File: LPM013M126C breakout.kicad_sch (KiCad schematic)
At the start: 9 parts, among them J1 Conn_01x12

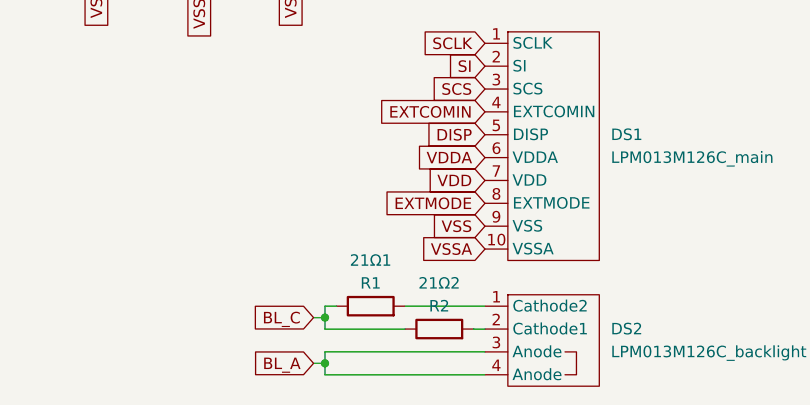
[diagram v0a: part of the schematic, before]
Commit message: fix references for R1, R2
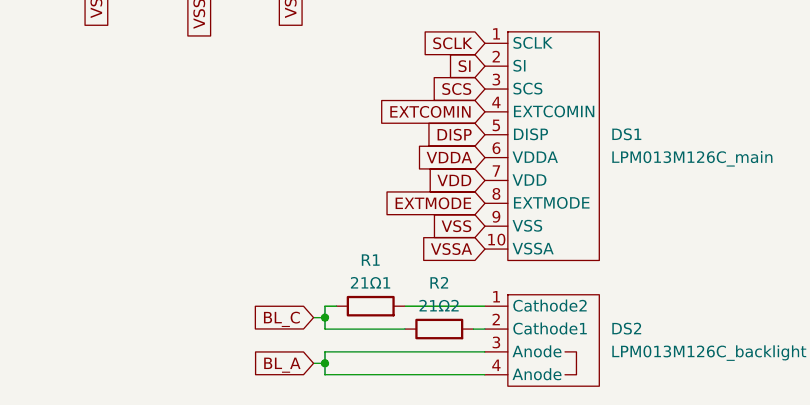
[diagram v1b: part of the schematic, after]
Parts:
- R1: renamed from 21Ω1; value R1 -> 21Ω1
- R2: renamed from 21Ω2; value R2 -> 21Ω2
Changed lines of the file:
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@@
   (symbol (lib_id "Device:R") (at 147.32 121.92 90) (unit 1)
     (in_bom yes) (on_board yes)
-    (property "Reference" "21Ω2" (id 0) (at 147.32 116.84 90))
-    (property "Value" "R2" (id 1) (at 147.32 119.38 90))
+    (property "Reference" "R2" (id 0) (at 147.32 116.84 90))
+    (property "Value" "21Ω2" (id 1) (at 147.32 119.38 90))
     (property "Footprint" "Resistor_SMD:R_0402_1005Metric" (id 2) (at 147.32 123.698 90)
       (effects (font (size 1.27 1.27)) hide)
@@
   (symbol (lib_id "Device:R") (at 139.7 119.38 90) (unit 1)
     (in_bom yes) (on_board yes)
-    (property "Reference" "21Ω1" (id 0) (at 139.7 114.3 90))
-    (property "Value" "R1" (id 1) (at 139.7 116.84 90))
+    (property "Reference" "R1" (id 0) (at 139.7 114.3 90))
+    (property "Value" "21Ω1" (id 1) (at 139.7 116.84 90))
     (property "Footprint" "Resistor_SMD:R_0402_1005Metric" (id 2) (at 139.7 115.57 90)
       (effects (font (size 1.27 1.27)) hide)
@@
   )
   (symbol_instances
-    (path "/c1a5108b-f59e-4cb8-bdc5-c79b8f1be77b"
-      (reference "21Ω1") (unit 1) (value "R1") (footprint "Resistor_SMD:R_0402_1005Metric")
-    )
-    (path "/a82829f9-f222-478e-854b-5b867f24f0f5"
-      (reference "21Ω2") (unit 1) (value "R2") (footprint "Resistor_SMD:R_0402_1005Metric")
-    )
     (path "/f411c12f-97f0-4a08-8aff-048f6ed3e203"
       (reference "C1") (unit 1) (value "0.1uF") (footprint "Capacitor_SMD:C_0402_1005Metric")
@@
       (reference "JP1") (unit 1) (value "SolderJumper_3_Open") (footprint "Jumper:SolderJumper-3_P1.3mm_Open_RoundedPad1.0x1.5mm_NumberLabels")
     )
+    (path "/c1a5108b-f59e-4cb8-bdc5-c79b8f1be77b"
+      (reference "R1") (unit 1) (value "21Ω1") (footprint "Resistor_SMD:R_0402_1005Metric")
+    )
+    (path "/a82829f9-f222-478e-854b-5b867f24f0f5"
+      (reference "R2") (unit 1) (value "21Ω2") (footprint "Resistor_SMD:R_0402_1005Metric")
+    )
   )

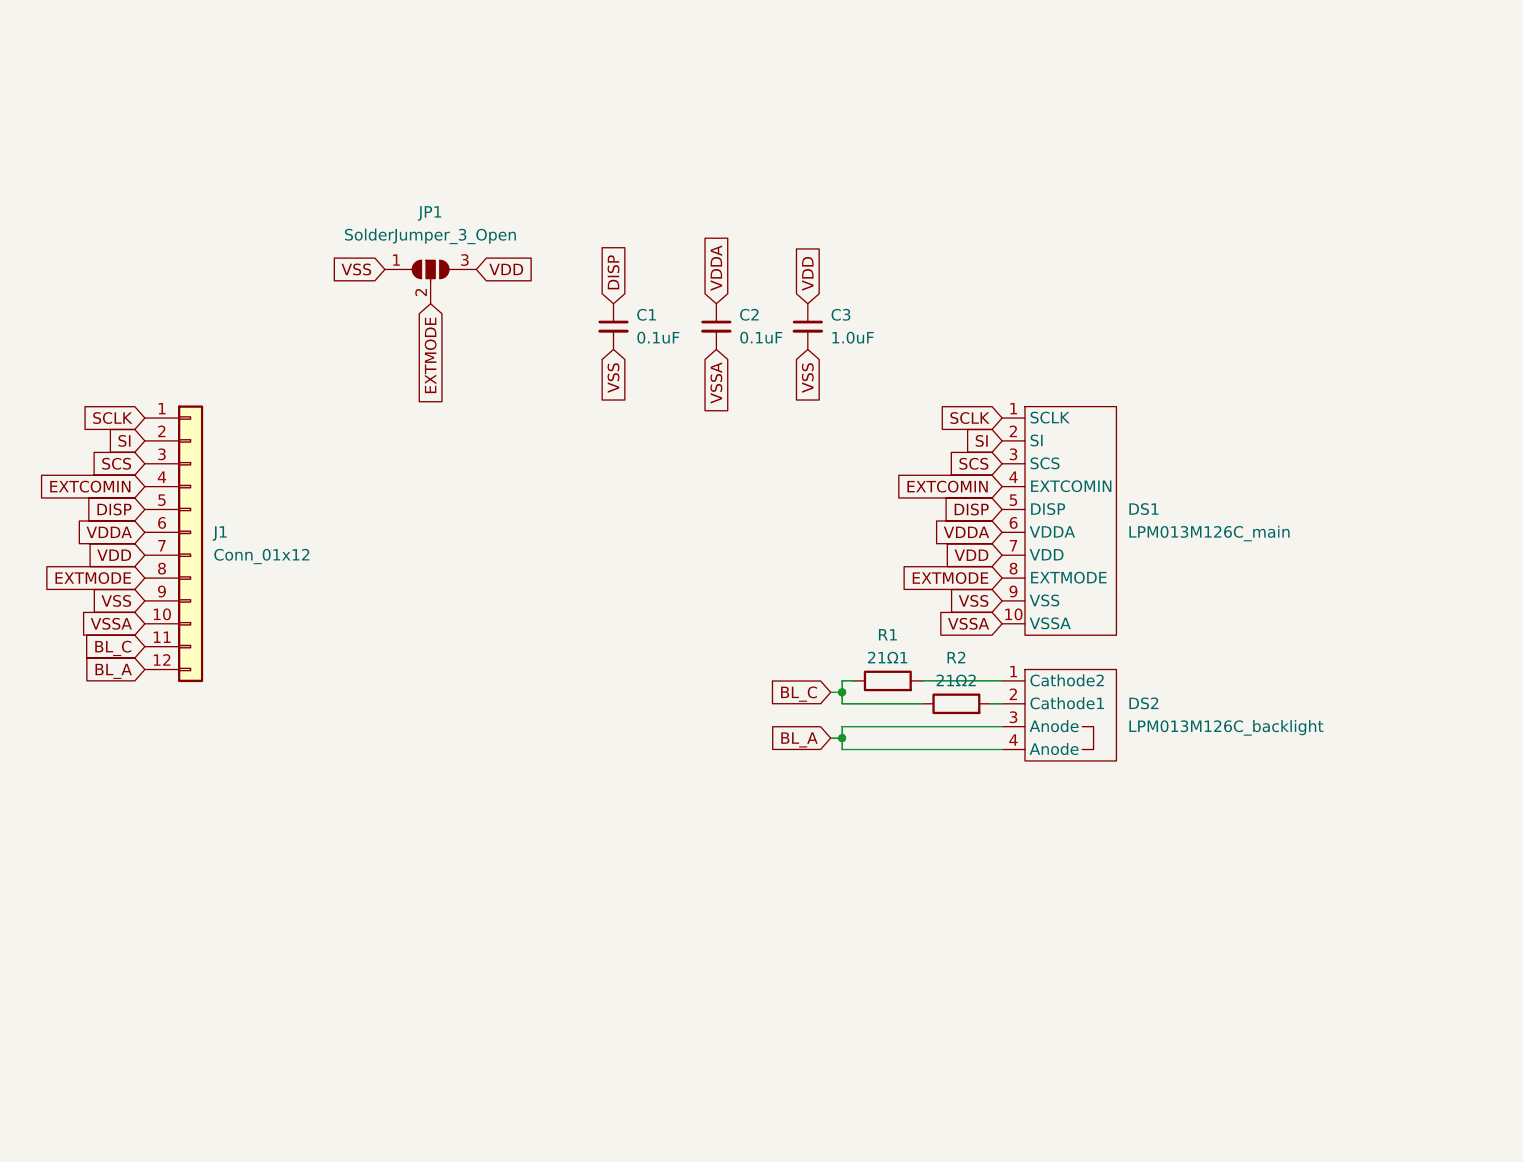
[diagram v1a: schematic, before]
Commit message: Add BJT for backlight
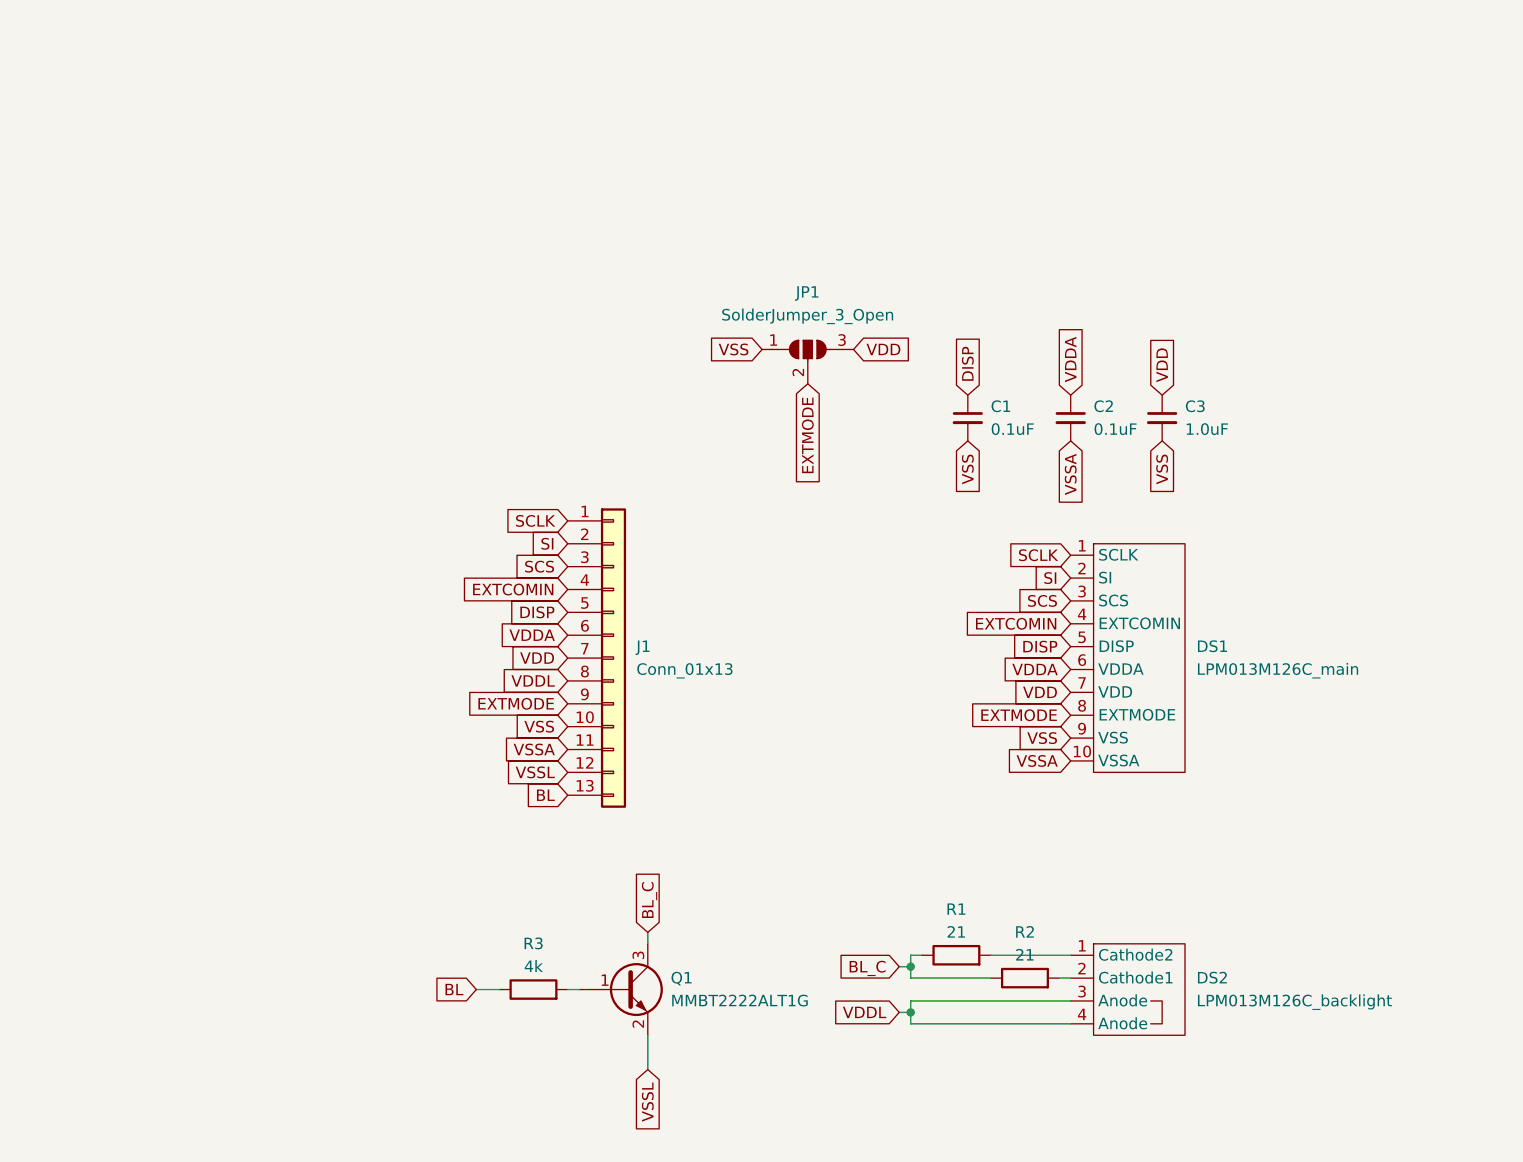
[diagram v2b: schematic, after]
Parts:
- removed J1: Conn_01x12, Connector_PinHeader_2.54mm:PinHeader_1x12_P2.54mm_Vertical, symbol Connector_Generic:Conn_01x12
- added J1: Conn_01x13, Connector_PinHeader_2.54mm:PinHeader_1x13_P2.54mm_Vertical, symbol Connector_Generic:Conn_01x13
- added Q1: MMBT2222ALT1G, Package_TO_SOT_SMD:SOT-23, symbol Custom_Transistor_BJT:MMBT2222ALT1G
- added R3: 4k, Resistor_SMD:R_0402_1005Metric, symbol Device:R
- R1: value 21Ω1 -> 21
- R2: value 21Ω2 -> 21
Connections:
- net BL_C: now also Q1.3 (C)
- net DISP: now also J1.5 (Pin_5)
- net EXTCOMIN: now also J1.4 (Pin_4)
- net EXTMODE: now also J1.9 (Pin_9)
- net SCLK: now also J1.1 (Pin_1)
- net SCS: now also J1.3 (Pin_3)
- net SI: now also J1.2 (Pin_2)
- net VDD: now also J1.7 (Pin_7)
- net VDDA: now also J1.6 (Pin_6)
- net VSS: now also J1.10 (Pin_10)
- net VSSA: now also J1.11 (Pin_11)
- net BL_A renamed VDDL
- net VDDL: now also J1.8 (Pin_8)
- new net: Q1.1 (B), R3.2
- new net BL: J1.13 (Pin_13), R3.1
- new net VSSL: J1.12 (Pin_12), Q1.2 (E)
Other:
- moved on the sheet: C1, C2, C3, DS1, DS2, JP1, R1, R2

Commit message: modified pipeline to only run DRC and ERC checks
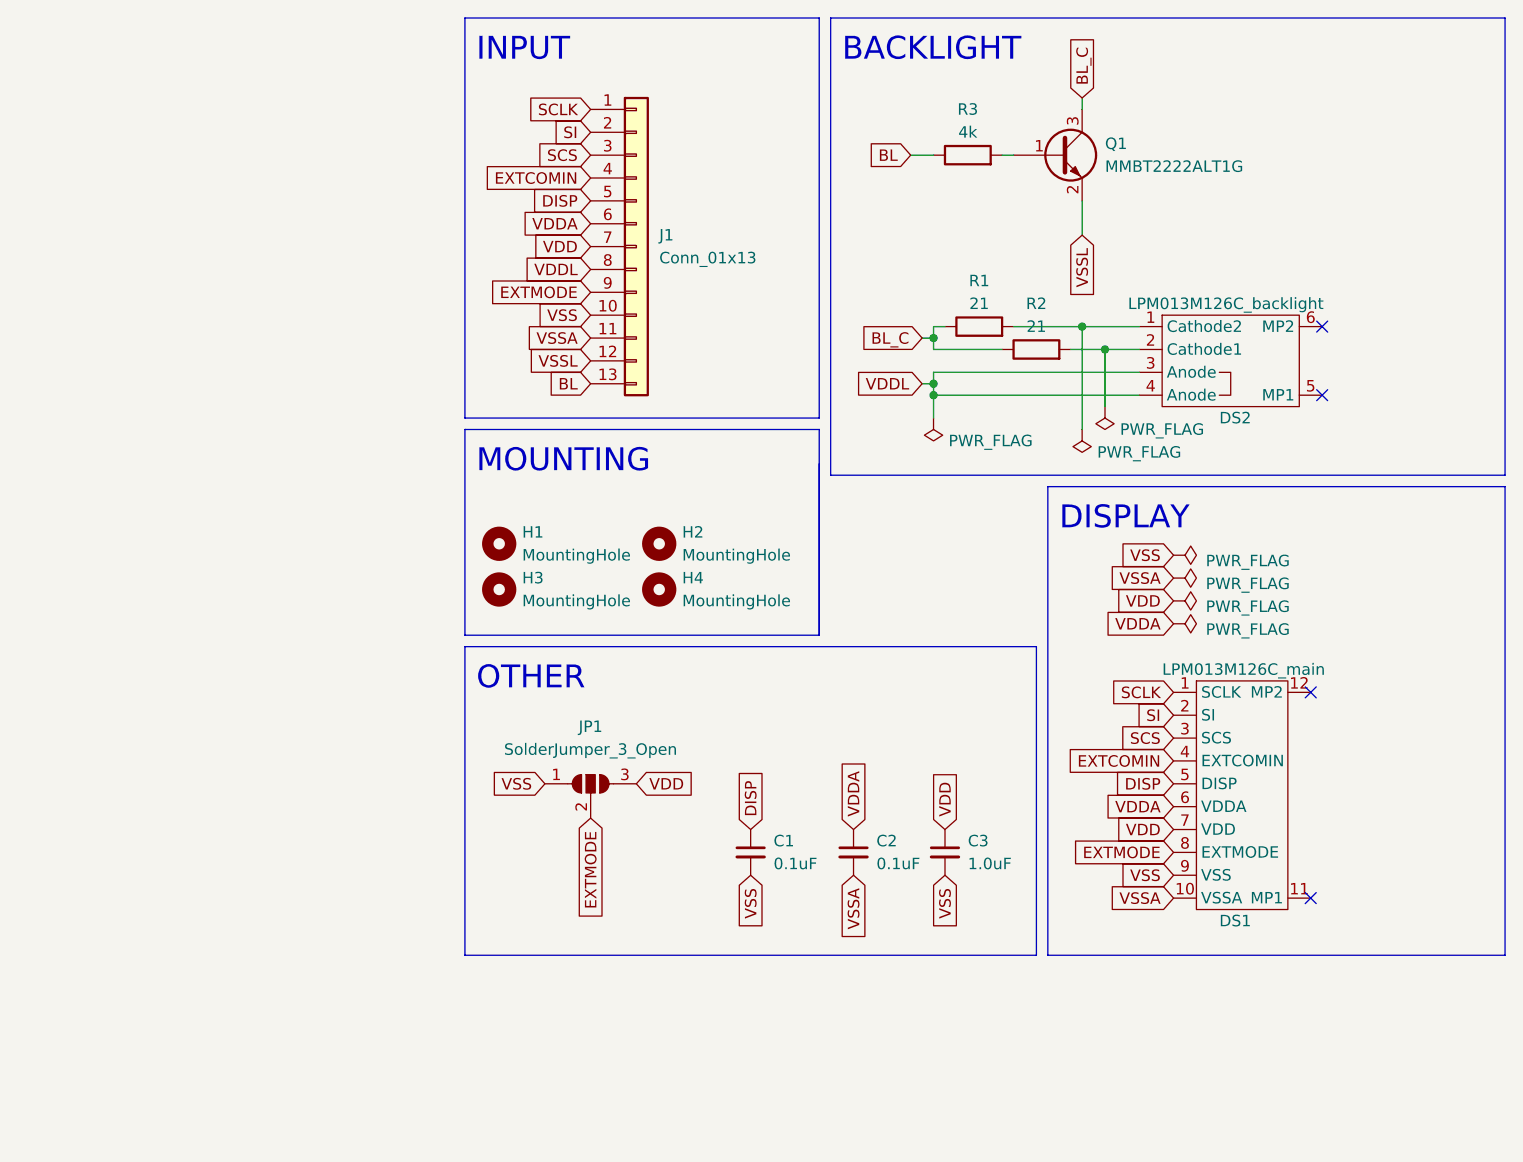
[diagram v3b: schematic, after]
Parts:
- added H1, H2, H3, H4: MountingHole, MountingHole:MountingHole_3.2mm_M3_ISO14580_Pad_TopBottom, symbol Mechanical:MountingHole
- DS2: Spice_Model (none) -> LPM013M126C_backlight; Spice_Netlist_Enabled (none) -> Y; Spice_Primitive (none) -> D
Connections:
- no-connect marks 0 -> 4
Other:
- note added: "BACKLIGHT"
- note added: "DISPLAY"
- note added: "INPUT"
- note added: "MOUNTING"
- note added: "OTHER"
- company: (none) -> testudor
- title: (none) -> LPM013M1126C breakout
- moved on the sheet: C1, C2, C3, J1, JP1, Q1, R1, R2, R3
